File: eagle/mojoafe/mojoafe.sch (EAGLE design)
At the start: 6 parts, among them IC1 MAX9939, IC2 MAX9939, IC3 MAX9939, J1 SMB50R, J2 SMB50R, J3 SMB50R

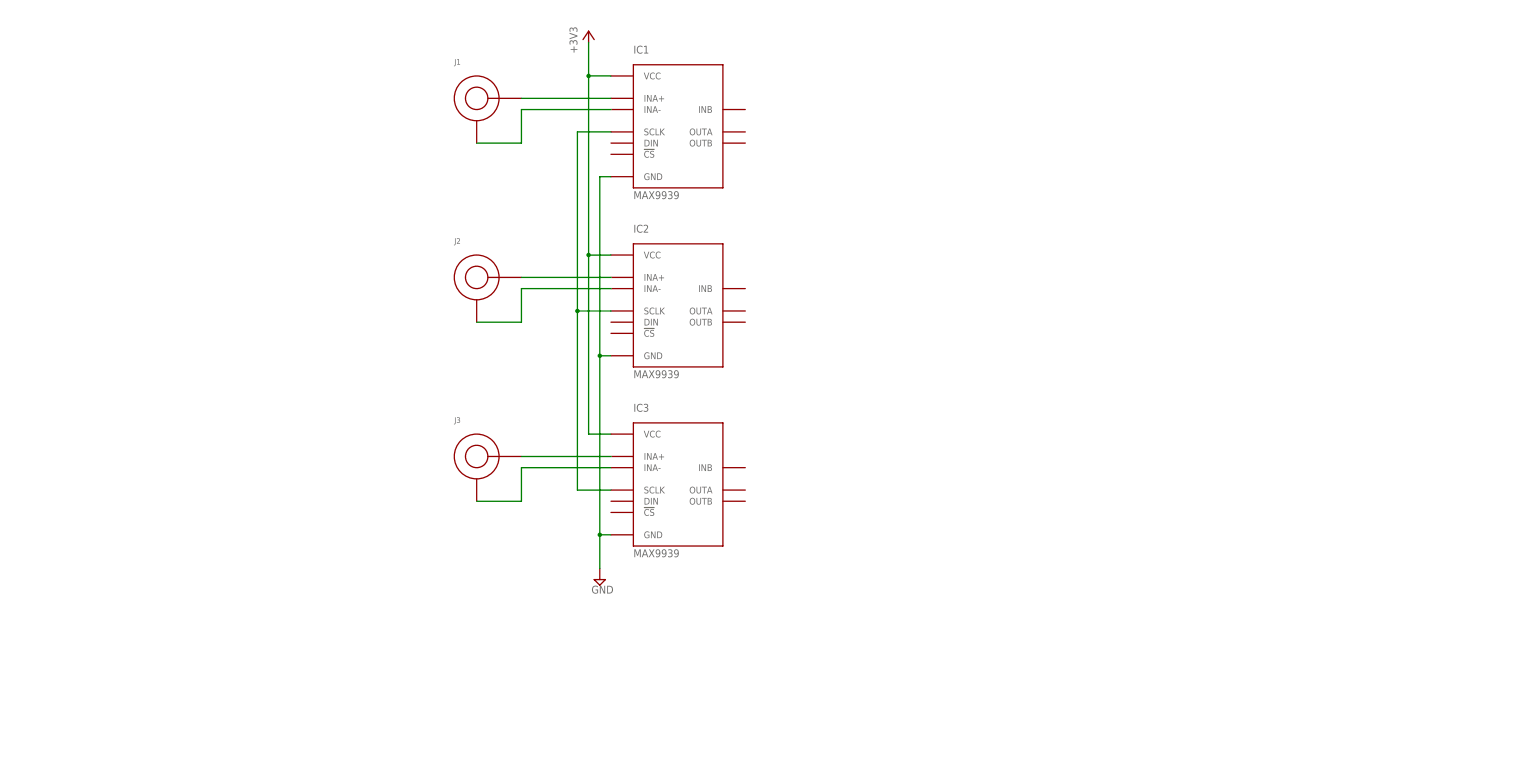
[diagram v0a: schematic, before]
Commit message: progress on mojo analog front-end
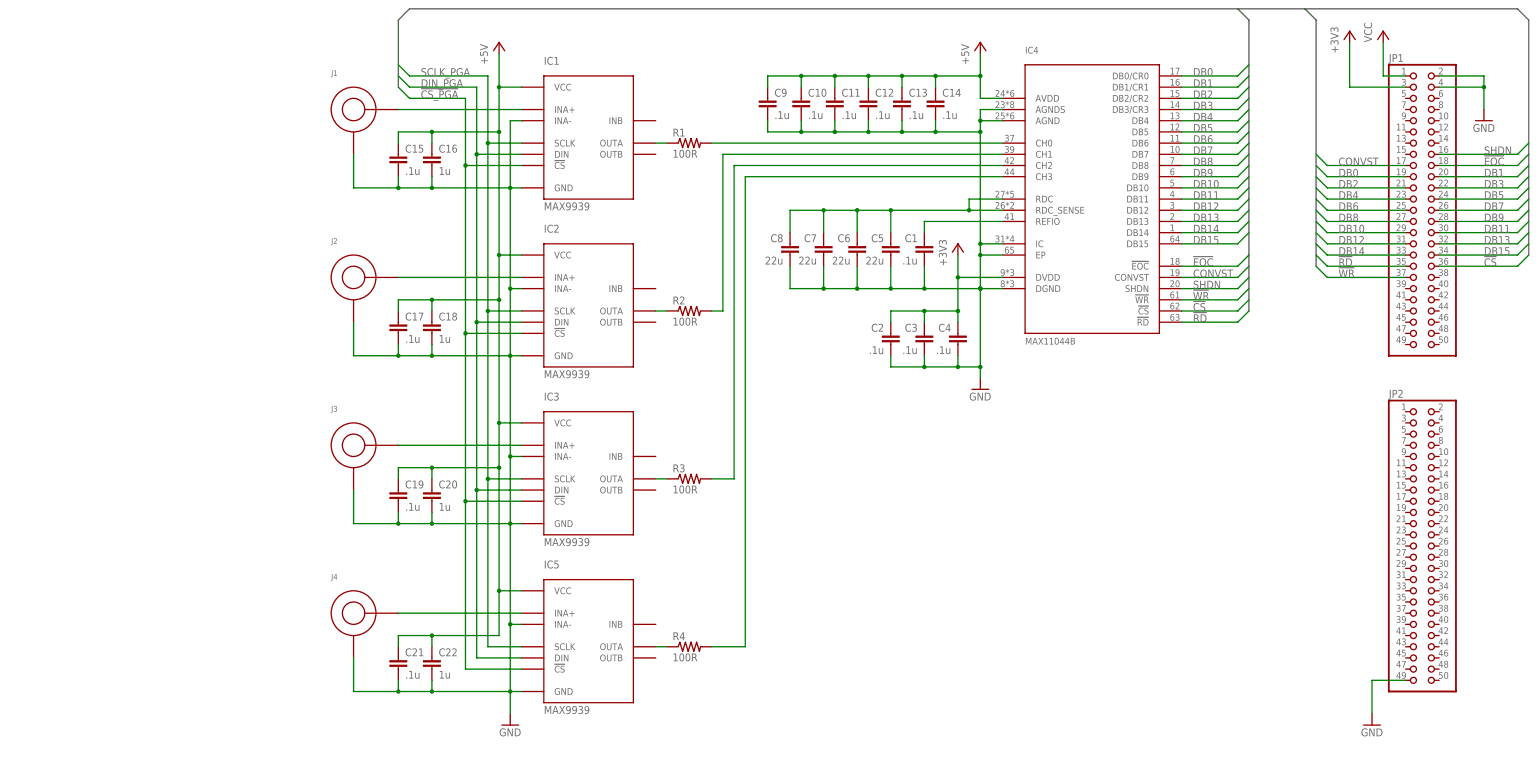
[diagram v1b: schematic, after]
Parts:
- added C1, C10, C11, C12, C13, C14, C15, C17, C19, C2, C21, C3, C4, C9: .1u, resistor:C-EUC0603K
- added C16, C18, C20, C22: 1u, resistor:C-EUC0603K
- added C5, C6, C7, C8: 22u, resistor:C-EUC0805K
- added IC4: MAX11044B, custom:MAX11044B
- added IC5: MAX9939, custom:MAX9939
- added J4: SMB50R, custom:SMB50R
- added JP1, JP2: (no value), pinhead:PINHD-2X25
- added R1, R2, R3, R4: 100R, resistor:R-US_R0603
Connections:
- removed net N$2: IC1.INA-, J1.1
- removed net N$3: IC2.INA-, J2.1
- removed net N$6: IC3.INA-, J3.1
- removed net N$7: IC1.SCLK, IC2.SCLK, IC3.SCLK
- new net !CS: IC4.!CS, JP1.36
- new net !CS_PGA: IC1.!CS, IC2.!CS, IC3.!CS, IC5.!CS
- new net !EOC: IC4.!EOC, JP1.18
- new net !RD: IC4.!RD, JP1.35
- new net !WR: IC4.!WR, JP1.37
- new net +5V: C10.1, C11.1, C12.1, C13.1, C14.1, C15.1, C16.1, C17.1, C18.1, C19.1, C20.1, C21.1, C22.1, C9.1, IC1.VCC, IC2.VCC, IC3.VCC, IC4.AVDD, IC5.VCC
- new net CONVST: IC4.CONVST, JP1.17
- new net DB0: IC4.DB0/CR0, JP1.19
- new net DB1: IC4.DB1/CR1, JP1.20
- new net DB10: IC4.DB10, JP1.29
- new net DB11: IC4.DB11, JP1.30
- new net DB12: IC4.DB12, JP1.31
- new net DB13: IC4.DB13, JP1.32
- new net DB14: IC4.DB14, JP1.33
- new net DB15: IC4.DB15, JP1.34
- new net DB2: IC4.DB2/CR2, JP1.21
- new net DB3: IC4.DB3/CR3, JP1.22
- new net DB4: IC4.DB4, JP1.23
- new net DB5: IC4.DB5, JP1.24
- new net DB6: IC4.DB6, JP1.25
- new net DB7: IC4.DB7, JP1.26
- new net DB8: IC4.DB8, JP1.27
- new net DB9: IC4.DB9, JP1.28
- new net DIN_PGA: IC1.DIN, IC2.DIN, IC3.DIN, IC5.DIN
- new net N$10: IC3.OUTA, R3.1
- new net N$11: IC5.OUTA, R4.1
- new net N$12: IC4.CH0, R1.2
- new net N$13: IC4.CH1, R2.2
- new net N$14: IC4.CH2, R3.2
- new net N$15: IC4.CH3, R4.2
- new net N$16: IC5.INA+, J4.2
- new net N$19: C5.1, C6.1, C7.1, C8.1, IC4.RDC, IC4.RDC_SENSE
- new net N$8: IC1.OUTA, R1.1
- new net N$9: IC2.OUTA, R2.1
- new net REFIO: C1.1, IC4.REFIO
- new net SCLK_PGA: IC1.SCLK, IC2.SCLK, IC3.SCLK, IC5.SCLK
- new net SHDN: IC4.SHDN, JP1.16
- new net VCC: JP1.1
- net +3V3: now also C2.1, C3.1, C4.1, IC4.DVDD, JP1.3; no longer IC1.VCC, IC2.VCC, IC3.VCC
- net GND: now also C1.2, C10.2, C11.2, C12.2, C13.2, C14.2, C15.2, C16.2, C17.2, C18.2, C19.2, C2.2, C20.2, C21.2, C22.2, C3.2, C4.2, C5.2, C6.2, C7.2, C8.2, C9.2, IC1.INA-, IC2.INA-, IC3.INA-, IC4.AGND, IC4.AGNDS, IC4.DGND, IC4.EP, IC4.IC, IC5.GND, IC5.INA-, J1.1, J2.1, J3.1, J4.1, JP1.2, JP1.4, JP2.49
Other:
- moved on the sheet: IC1, IC2, IC3, J1, J2, J3

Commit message: finished mojo afe PCB, generated CAM files and BoM
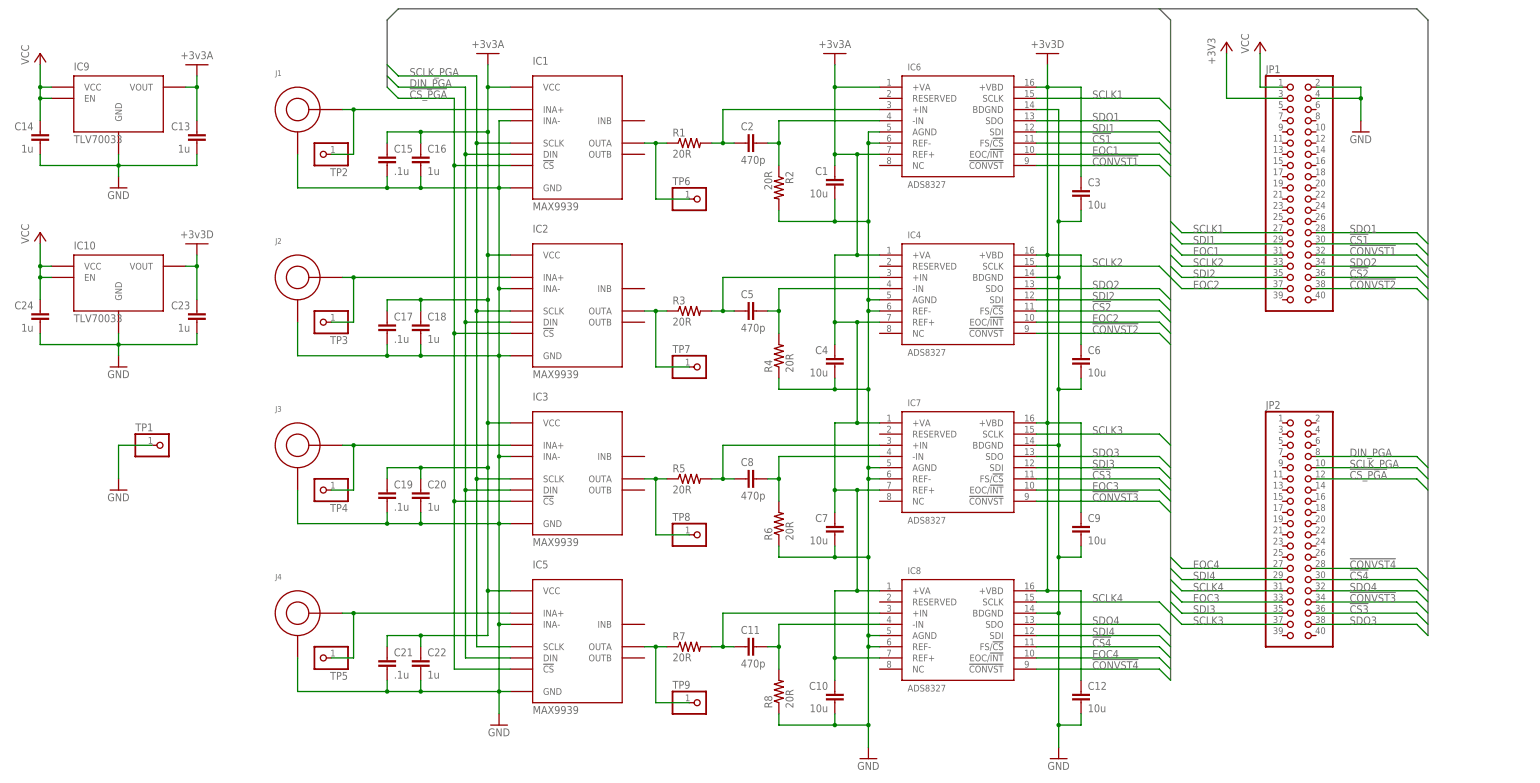
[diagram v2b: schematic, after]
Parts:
- added C23, C24: 1u, resistor:C-EUC0603K
- added IC10, IC9: TLV70033, custom:TLV70033
- added IC6, IC7, IC8: ADS8327, custom:ADS8327
- added R5, R6, R7, R8: 20R, resistor:R-US_R0603
- added TP1, TP2, TP3, TP4, TP5, TP6, TP7, TP8, TP9: (no value), pinhead:PINHD-1X1
- C1, C10, C12, C3, C4, C9: value .1u -> 10u
- C11, C2: value .1u -> 470p
- C13, C14: value .1u -> 1u
- C5, C8: value 22u -> 470p; device resistor:C-EUC0805K -> resistor:C-EUC0603K
- C6, C7: value 22u -> 10u; device resistor:C-EUC0805K -> resistor:C-EUC0603K
- IC4: value MAX11044B -> ADS8327; device custom:MAX11044B -> custom:ADS8327
- JP1, JP2: device pinhead:PINHD-2X25 -> pinhead:PINHD-2X20
- R1, R2, R3, R4: value 100R -> 20R
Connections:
- removed net !CS: IC4.!CS, JP1.36
- removed net !EOC: IC4.!EOC, JP1.18
- removed net !RD: IC4.!RD, JP1.35
- removed net !WR: IC4.!WR, JP1.37
- removed net +5V: C10.1, C11.1, C12.1, C13.1, C14.1, C15.1, C16.1, C17.1, C18.1, C19.1, C20.1, C21.1, C22.1, C9.1, IC1.VCC, IC2.VCC, IC3.VCC, IC4.AVDD, IC5.VCC
- removed net CONVST: IC4.CONVST, JP1.17
- removed net DB0: IC4.DB0/CR0, JP1.19
- removed net DB1: IC4.DB1/CR1, JP1.20
- removed net DB10: IC4.DB10, JP1.29
- removed net DB11: IC4.DB11, JP1.30
- removed net DB12: IC4.DB12, JP1.31
- removed net DB13: IC4.DB13, JP1.32
- removed net DB14: IC4.DB14, JP1.33
- removed net DB15: IC4.DB15, JP1.34
- removed net DB2: IC4.DB2/CR2, JP1.21
- removed net DB3: IC4.DB3/CR3, JP1.22
- removed net DB4: IC4.DB4, JP1.23
- removed net DB5: IC4.DB5, JP1.24
- removed net DB6: IC4.DB6, JP1.25
- removed net DB7: IC4.DB7, JP1.26
- removed net DB8: IC4.DB8, JP1.27
- removed net DB9: IC4.DB9, JP1.28
- removed net N$11: IC5.OUTA, R4.1
- removed net REFIO: C1.1, IC4.REFIO
- removed net SHDN: IC4.SHDN, JP1.16
- new net !CONVST1: IC6.!CONVST, JP1.32
- new net !CONVST2: IC4.!CONVST, JP1.38
- new net !CONVST3: IC7.!CONVST, JP2.34
- new net !CONVST4: IC8.!CONVST, JP2.28
- new net !CS1: IC6.FS/!CS, JP1.30
- new net !CS2: IC4.FS/!CS, JP1.36
- new net !CS3: IC7.FS/!CS, JP2.36
- new net !CS4: IC8.FS/!CS, JP2.30
- new net +3V3A: C1.1, C10.1, C13.1, C15.1, C16.1, C17.1, C18.1, C19.1, C20.1, C21.1, C22.1, C4.1, C7.1, IC1.VCC, IC2.VCC, IC3.VCC, IC4.+VA, IC4.REF+, IC5.VCC, IC6.+VA, IC6.REF+, IC7.+VA, IC7.REF+, IC8.+VA, IC8.REF+, IC9.VOUT
- new net +3V3D: C12.1, C23.1, C3.1, C6.1, C9.1, IC10.VOUT, IC4.+VBD, IC6.+VBD, IC7.+VBD, IC8.+VBD
- new net EOC1: IC6.EOC/!INT, JP1.31
- new net EOC2: IC4.EOC/!INT, JP1.37
- new net EOC3: IC7.EOC/!INT, JP2.33
- new net EOC4: IC8.EOC/!INT, JP2.27
- new net N$2: IC3.OUTA, R5.1, TP8.1
- new net N$22: C11.2, IC8.-IN, R8.2
- new net N$3: C8.2, IC7.-IN, R6.2
- new net N$6: IC5.OUTA, R7.1, TP9.1
- new net SCLK1: IC6.SCLK, JP1.27
- new net SCLK2: IC4.SCLK, JP1.33
- new net SCLK3: IC7.SCLK, JP2.37
- new net SCLK4: IC8.SCLK, JP2.31
- new net SDI1: IC6.SDI, JP1.29
- new net SDI2: IC4.SDI, JP1.35
- new net SDI3: IC7.SDI, JP2.35
- new net SDI4: IC8.SDI, JP2.29
- new net SDO1: IC6.SDO, JP1.28
- new net SDO2: IC4.SDO, JP1.34
- new net SDO3: IC7.SDO, JP2.38
- new net SDO4: IC8.SDO, JP2.32
- net !CS_PGA: now also JP2.12
- net +3V3: no longer C2.1, C3.1, C4.1, IC4.DVDD
- net DIN_PGA: now also JP2.8
- net GND: now also C23.2, C24.2, IC10.GND, IC4.BDGND, IC4.REF-, IC6.AGND, IC6.BDGND, IC6.REF-, IC7.AGND, IC7.BDGND, IC7.REF-, IC8.AGND, IC8.BDGND, IC8.REF-, IC9.GND, R2.2, R4.1, R6.1, R8.1, TP1.1; no longer C11.2, C2.2, C5.2, C8.2, IC4.AGNDS, IC4.DGND, IC4.EP, IC4.IC, JP2.49
- net N$1: now also TP2.1
- net N$10: now also C5.1, IC4.+IN, R3.2; no longer IC3.OUTA, R3.1
- net N$12: now also C2.1, IC6.+IN; no longer IC4.CH0
- net N$13: now also C5.2, IC4.-IN, R4.2; no longer IC4.CH1, R2.2
- net N$14: now also C2.2, IC6.-IN, R2.1; no longer IC4.CH2, R3.2
- net N$15: now also C8.1, IC7.+IN, R5.2; no longer IC4.CH3, R4.2
- net N$16: now also TP5.1
- net N$19: now also C11.1, IC8.+IN, R7.2; no longer C5.1, C6.1, C7.1, C8.1, IC4.RDC, IC4.RDC_SENSE
- net N$4: now also TP3.1
- net N$5: now also TP4.1
- net N$8: now also TP6.1
- net N$9: now also R3.1, TP7.1; no longer R2.1
- net SCLK_PGA: now also JP2.10
- net VCC: now also C14.1, C24.1, IC10.EN, IC10.VCC, IC9.EN, IC9.VCC
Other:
- moved on the sheet: C1, C10, C11, C12, C13, C14, C15, C16, C17, C18, C19, C2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

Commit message: rev 5.7.14 complete, sent for production
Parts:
- IC4: value ADS8327 -> MAX9939; device custom:ADS8327 -> custom:MAX9939
- IC5: value MAX9939 -> ADS8327; device custom:MAX9939 -> custom:ADS8327
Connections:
- net !CONVST1: now also IC5.!CONVST; no longer IC6.!CONVST
- net !CONVST2: now also IC6.!CONVST; no longer IC4.!CONVST
- net !CS1: now also IC5.FS/!CS; no longer IC6.FS/!CS
- net !CS2: now also IC6.FS/!CS; no longer IC4.FS/!CS
- net !CS_PGA: now also IC4.!CS; no longer IC5.!CS
- net +3V3A: now also IC4.VCC, IC5.+VA, IC5.REF+; no longer IC4.+VA, IC4.REF+, IC5.VCC
- net +3V3D: now also IC5.+VBD; no longer IC4.+VBD
- net DIN_PGA: now also IC4.DIN; no longer IC5.DIN
- net EOC1: now also IC5.EOC/!INT; no longer IC6.EOC/!INT
- net EOC2: now also IC6.EOC/!INT; no longer IC4.EOC/!INT
- net GND: now also IC4.GND, IC4.INA-, IC5.AGND, IC5.BDGND, IC5.REF-; no longer IC4.AGND, IC4.BDGND, IC4.REF-, IC5.GND, IC5.INA-
- net N$10: now also IC6.+IN; no longer IC4.+IN
- net N$12: now also IC5.+IN; no longer IC6.+IN
- net N$13: now also IC6.-IN; no longer IC4.-IN
- net N$14: now also IC5.-IN; no longer IC6.-IN
- net N$16: now also IC4.INA+; no longer IC5.INA+
- net N$6: now also IC4.OUTA; no longer IC5.OUTA
- net SCLK1: now also IC5.SCLK; no longer IC6.SCLK
- net SCLK2: now also IC6.SCLK; no longer IC4.SCLK
- net SCLK_PGA: now also IC4.SCLK; no longer IC5.SCLK
- net SDI1: now also IC5.SDI; no longer IC6.SDI
- net SDI2: now also IC6.SDI; no longer IC4.SDI
- net SDO1: now also IC5.SDO; no longer IC6.SDO
- net SDO2: now also IC6.SDO; no longer IC4.SDO
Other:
- moved on the sheet: IC6
